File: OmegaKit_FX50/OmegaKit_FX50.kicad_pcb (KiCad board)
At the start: 2 copper layers, 92.5 x 48 mm, 29 parts, among them U1 ESP32-DEVKIT-V1, U2 AMS1117-3.3

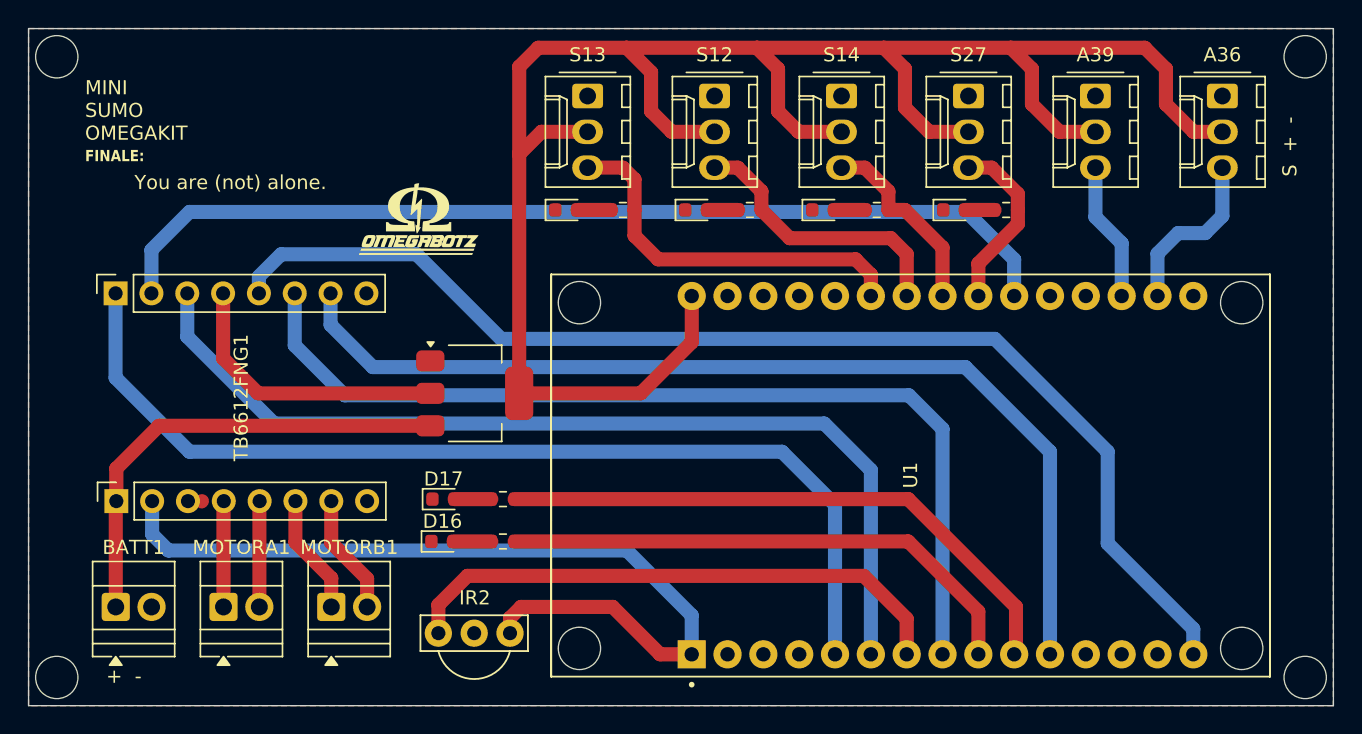
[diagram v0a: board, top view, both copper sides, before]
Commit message: Ajustes regulador de tensão + switch e capacitor + não usar pinoGPIO12
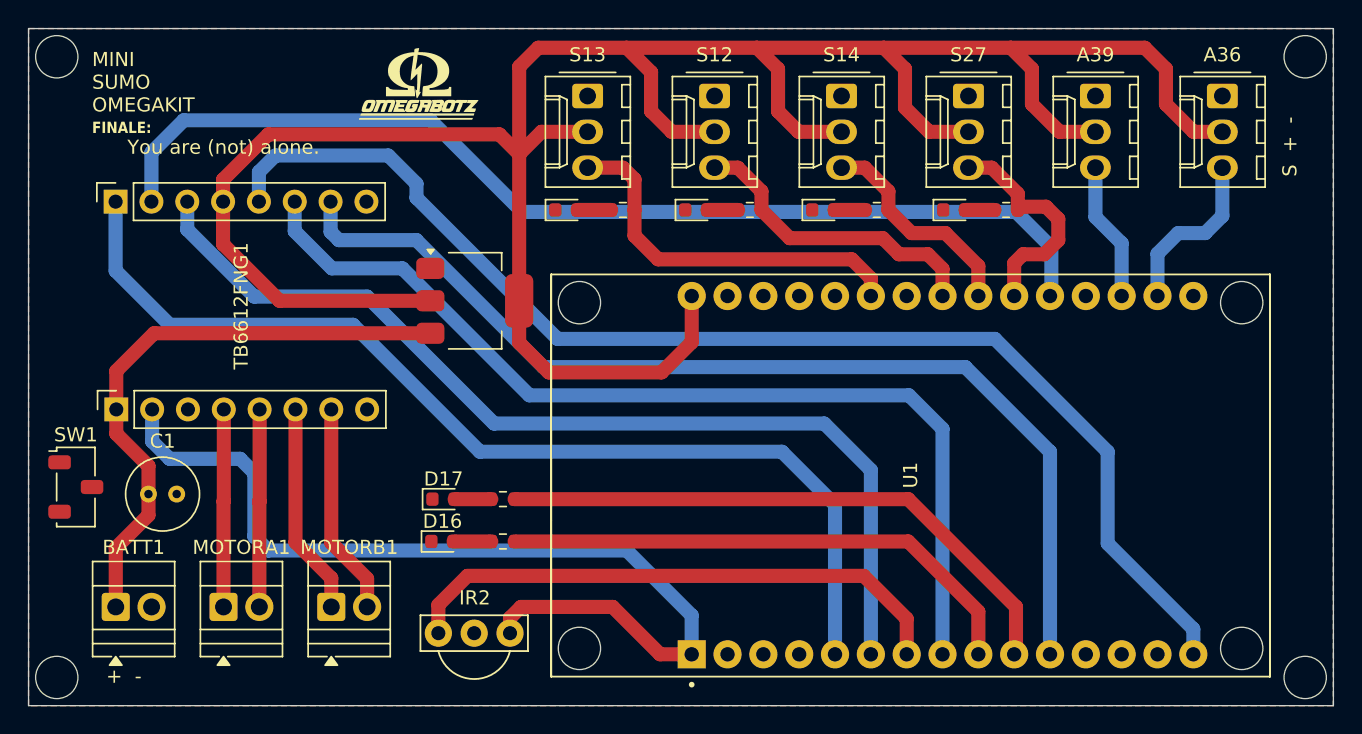
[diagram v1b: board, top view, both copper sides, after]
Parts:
- added C1: C_US, Capacitor_THT:C_Radial_D5.0mm_H5.0mm_P2.00mm, F.Cu at (90.0, 108.0)
- added SW1: SW_Nidec_CAS-120A1, Button_Switch_SMD:Nidec_Copal_CAS-120A, F.Cu at (84.8, 107.5)
- BATT1, MOTORA1, MOTORB1: value Screw_Terminal_01x02 -> Borne
- moved U2 6.56 mm to (113.1, 94.3)
- moved TB6612FNG1 6.50 mm to (87.7, 102.0)
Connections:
- U1 pad 20: unconnected-(U1-D35-Pad20) -> /AIN2
- U1 pad 21: /AIN2 -> /S1
- U1 pad 22: /S1 -> /S2
- U1 pad 23: /S2 -> /S3
- U1 pad 24: /S3 -> unconnected-(U1-D26-Pad24)
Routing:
- net /V_REG: track 160.9 -> 181.1 mm
- net /BATT_VCC: track 33.3 -> 42.4 mm
- net /A_VCC: track 7.48 -> 14.0 mm
- net /A_GND: track 7.48 -> 14.0 mm
- net /B_VCC: track 8.55 -> 15.1 mm
- net /B_GND: track 8.55 -> 15.1 mm
- net /AIN2: track 69.3 -> 75.4 mm
- net /VCC: track 61.4 -> 66.7 mm
- net /BIN1: track 84.7 -> 88.9 mm
- net /S1: track 12.7 -> 16.4 mm
- net /PWMB: track 71.3 -> 74.0 mm
- net /PWMA: track 71.3 -> 73.4 mm
- net /AIN1: track 68.5 -> 70.6 mm
- net /S3: track 19.9 -> 21.8 mm
- net /S2: track 13.7 -> 15.5 mm
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
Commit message: Correção de pinos + novas plotagens + modelos step + gerbers
Co-authored-by: rarolle <rarolle@gmail.com>
Co-authored-by: RafaHR <rafahramos02@gmail.com>
Co-authored-by: Guilherme36 <guilherminhofeh@hotmail.com>
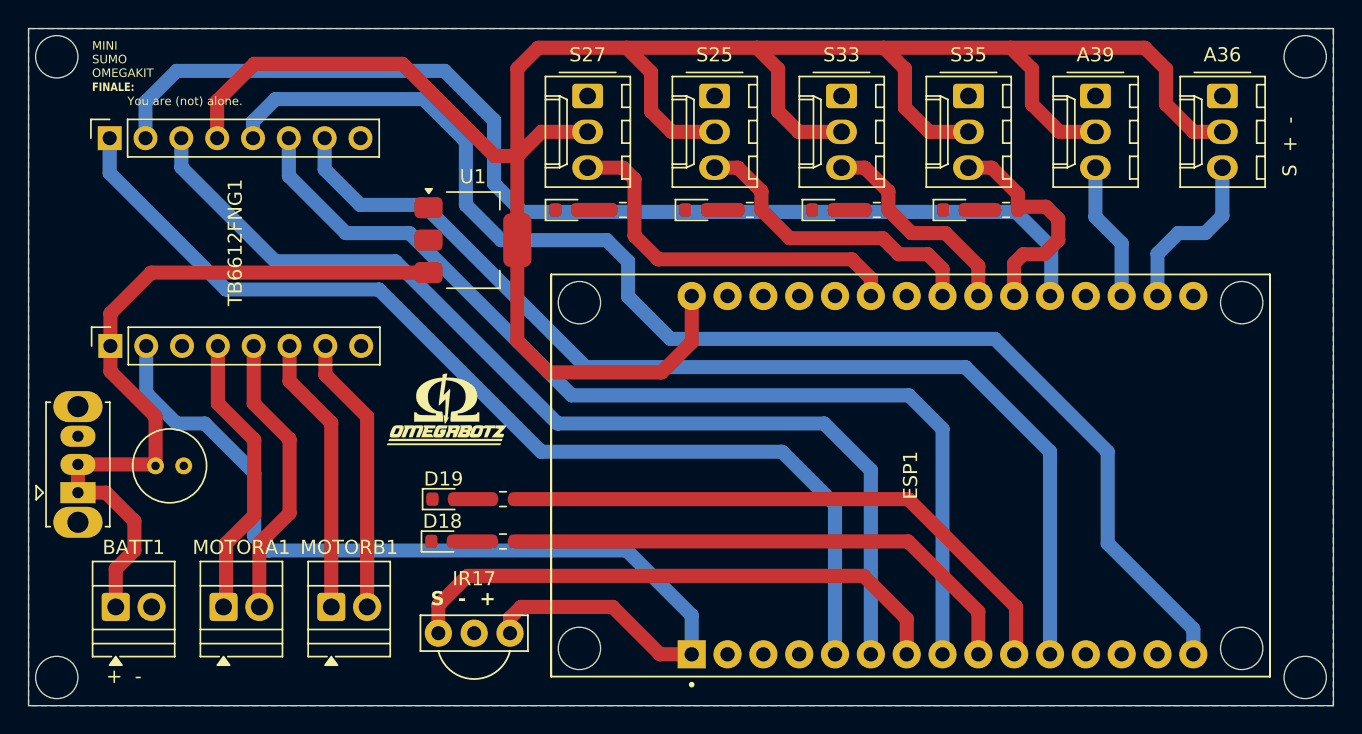
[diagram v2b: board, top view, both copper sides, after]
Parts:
- removed U2: AMS1117-3.3, Package_TO_SOT_SMD:SOT-223-3_TabPin2
- added U1: AMS1117-5.0, Package_TO_SOT_SMD:SOT-223-3_TabPin2, F.Cu at (113.0, 90.0)
- SW1: value SW_Nidec_CAS-120A1 -> SW_CK_OS102011MS2Q; footprint Button_Switch_SMD:Nidec_Copal_CAS-120A -> Button_Switch_THT:SW_Slide_SPDT_Straight_CK_OS102011MS2Q
- moved TB6612FNG1 4.52 mm to (87.3, 97.5)
- moved C1 2.06 mm to (90.5, 106.0)
- moved SW1 0.43 mm to (85.0, 107.9), turned to 90 degrees
- renumbered D16 to D18, D17 to D19, U1 to ESP1, IR2 to IR17, S12 to S25, S13 to S27, S14 to S33, S27 to S35
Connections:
- SW1 pad 1: GND -> /BATT_VCC
- SW1 pad 2: GND -> /BATT_VCC
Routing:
- net /V_REG: track 181.1 -> 165.2 mm
- net /BATT_VCC: track 42.4 -> 54.9 mm
- net /A_VCC: track 14.0 -> 20.5 mm
- net /A_GND: track 14.0 -> 20.4 mm
- net /BIN1: track 88.9 -> 93.8 mm
- net /B_VCC: track 15.1 -> 19.7 mm
- net /B_GND: track 15.1 -> 19.7 mm
- net /AIN2: track 75.4 -> 79.0 mm
- net /VCC: track 66.7 -> 69.6 mm
- net /BIN2: track 69.8 -> 72.4 mm
- net /PWMB: track 74.0 -> 76.3 mm
- net /AIN1: track 70.6 -> 72.9 mm
- net /PWMA: track 73.4 -> 74.2 mm
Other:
- board text added: "S - +"

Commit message: ✨ feat: atualização de todos os arquivps faltantes
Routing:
- net /V_REG: track 165.2 -> 172.1 mm
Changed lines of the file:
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@@
 			(at 0 0 90)
 			(layer "F.SilkS")
+			(hide yes)
 			(effects
 				(font
@@
 	)
 	(segment
-		(start 114.53 84.03)
-		(end 108 77.5)
+		(start 94.87 80.13)
+		(end 94.87 82.77)
 		(width 1)
 		(layer "F.Cu")
@@
 	)
 	(segment
-		(start 117.86 82.32)
-		(end 121.13 82.32)
-		(width 1)
-		(layer "F.Cu")
-		(net 37)
-	)
-	(segment
 		(start 164.09 82.32)
 		(end 166.13 82.32)
@@
 	)
 	(segment
-		(start 94.87 80.13)
-		(end 94.87 82.77)
+		(start 105 77.5)
+		(end 97.5 77.5)
 		(width 1)
 		(layer "F.Cu")
@@
 	)
 	(segment
+		(start 97.5 77.5)
+		(end 94.87 80.13)
+		(width 1)
+		(layer "F.Cu")
+		(net 37)
+	)
+	(segment
+		(start 111.53 84.03)
+		(end 105 77.5)
+		(width 1)
+		(layer "F.Cu")
+		(net 37)
+	)
+	(segment
 		(start 154.59 82.32)
 		(end 157.13 82.32)
@@
 	)
 	(segment
-		(start 108 77.5)
-		(end 97.5 77.5)
-		(width 1)
-		(layer "F.Cu")
-		(net 37)
-	)
-	(segment
 		(start 125.63 78.096844)
 		(end 125.63 80.86)
@@
 	)
 	(segment
+		(start 116.15 83.09)
+		(end 116.92 82.32)
+		(width 1)
+		(layer "F.Cu")
+		(net 37)
+	)
+	(segment
 		(start 136.09 82.32)
 		(end 139.13 82.32)
@@
 	(segment
 		(start 116.15 84.03)
-		(end 117.86 82.32)
+		(end 111.53 84.03)
+		(width 1)
+		(layer "F.Cu")
+		(net 37)
+	)
+	(segment
+		(start 109.85 90)
+		(end 116.15 90)
+		(width 1)
+		(layer "F.Cu")
+		(net 37)
+	)
+	(segment
+		(start 116.92 82.32)
+		(end 121.13 82.32)
 		(width 1)
 		(layer "F.Cu")
@@
 	)
 	(segment
-		(start 116.15 84.03)
-		(end 114.53 84.03)
-		(width 1)
-		(layer "F.Cu")
-		(net 37)
-	)
-	(segment
-		(start 97.5 77.5)
-		(end 94.87 80.13)
+		(start 142.13 76.36)
+		(end 143.63 77.86)
 		(width 1)
 		(layer "F.Cu")
@@
 	)
 	(segment
-		(start 142.13 76.36)
-		(end 143.63 77.86)
+		(start 116.15 84.03)
+		(end 116.15 83.09)
 		(width 1)
 		(layer "F.Cu")
